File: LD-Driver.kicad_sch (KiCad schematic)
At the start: 2 parts, among them J1 BASYS3, U1 MCP4728

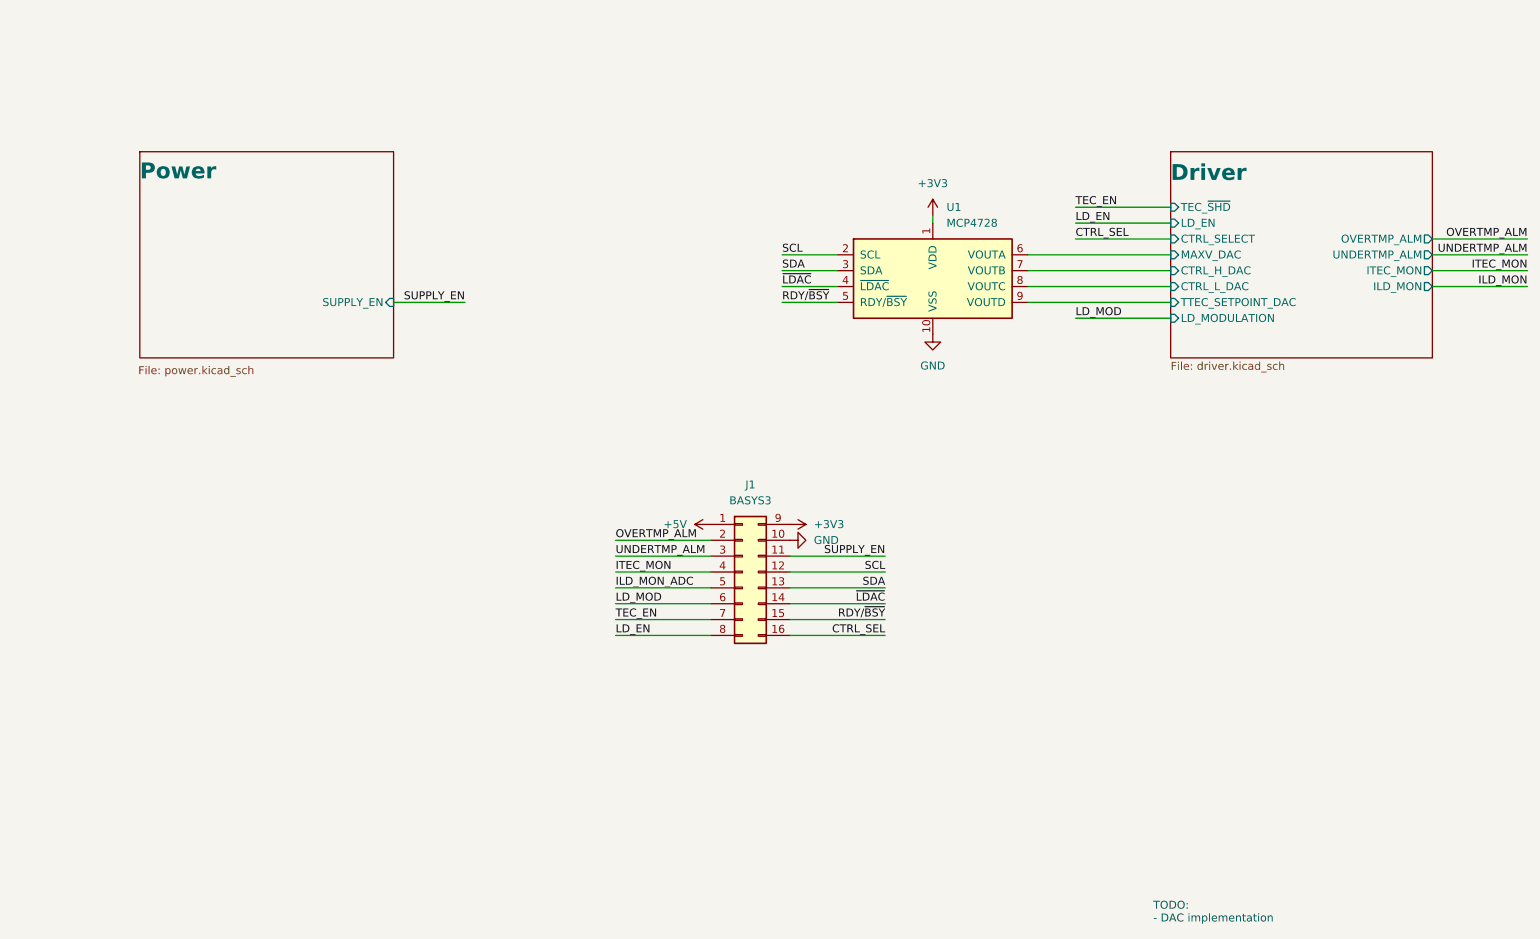
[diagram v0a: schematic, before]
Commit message: update PCB: fixed buck layout, concept layout for LD driver with LT3743
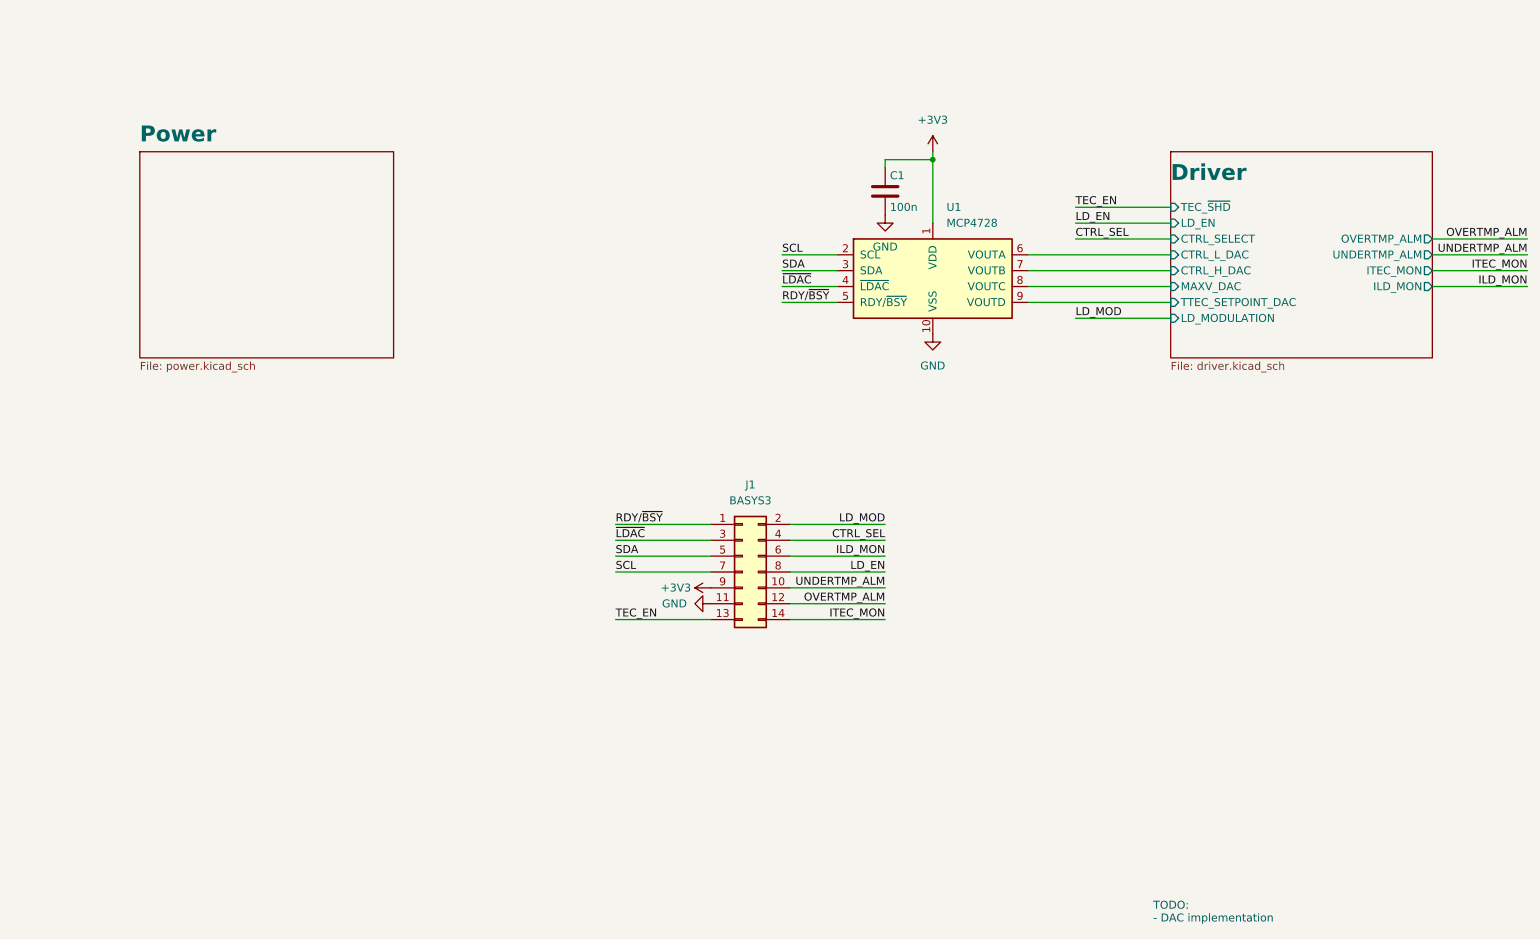
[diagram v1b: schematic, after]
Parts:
- added C1: 100n, Capacitor_SMD:C_0805_2012Metric, symbol Device:C
- J1: footprint Connector_PinHeader_2.54mm:PinHeader_2x08_P2.54mm_Horizontal -> Connector_PinHeader_2.54mm:PinHeader_2x07_P2.54mm_Horizontal; symbol Connector_Generic:Conn_02x08_Top_Bottom -> Connector_Generic:Conn_02x07_Odd_Even
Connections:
- net +5V is gone; now on net RDY/~{BSY}: J1.1 (Pin_1)
- net ILD_MON_ADC is gone; now on net SDA: J1.5 (Pin_5)
- net SUPPLY_EN is gone; now on net GND: J1.11 (Pin_11)
- net +3V3: now also C1.1
- net CTRL_SEL: now also J1.4 (Pin_4); no longer J1.16 (Pin_16)
- net Driver/CTRL_L_DAC: now also U1.6 (VOUTA); no longer U1.8 (VOUTC)
- net Driver/MAXV_DAC: now also U1.8 (VOUTC); no longer U1.6 (VOUTA)
- net GND: now also C1.2; no longer J1.10 (Pin_10)
- net ILD_MON: now also J1.6 (Pin_6)
- net ITEC_MON: now also J1.14 (Pin_14); no longer J1.4 (Pin_4)
- net LD_MOD: now also J1.2 (Pin_2); no longer J1.6 (Pin_6)
- net OVERTMP_ALM: now also J1.12 (Pin_12); no longer J1.2 (Pin_2)
- net RDY/~{BSY}: no longer J1.15 (Pin_15)
- net SCL: now also J1.7 (Pin_7); no longer J1.12 (Pin_12)
- net SDA: no longer J1.13 (Pin_13)
- net TEC_EN: now also J1.13 (Pin_13); no longer J1.7 (Pin_7)
- net UNDERTMP_ALM: now also J1.10 (Pin_10); no longer J1.3 (Pin_3)
- net ~{LDAC}: now also J1.3 (Pin_3); no longer J1.14 (Pin_14)
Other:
- sheet Power ports: added none; removed SUPPLY_EN

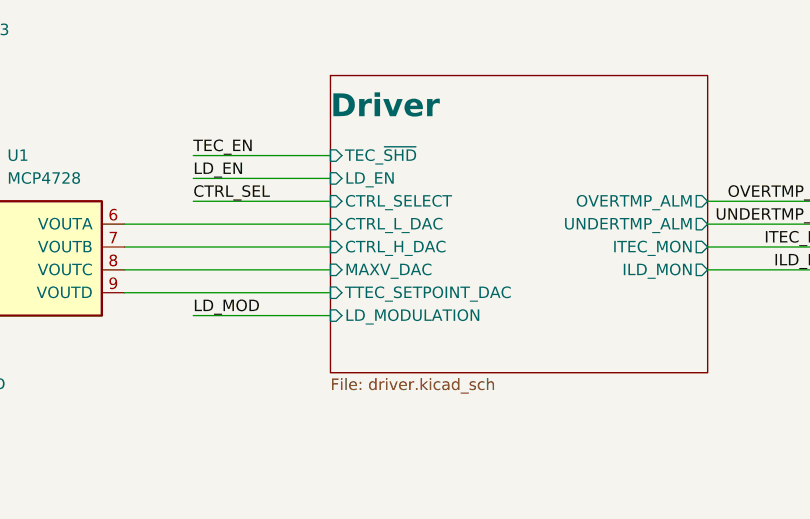
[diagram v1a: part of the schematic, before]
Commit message: PCB routing completed, started uniforming components for smaller BOM
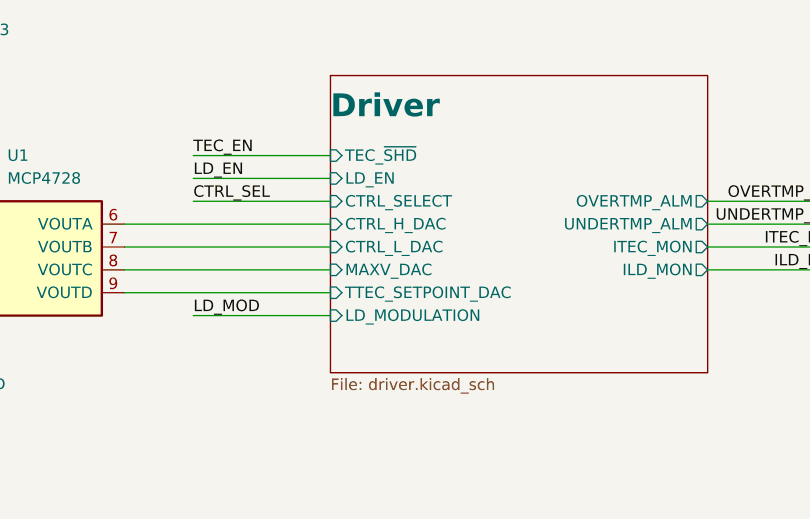
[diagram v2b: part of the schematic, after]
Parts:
- C1: footprint Capacitor_SMD:C_0805_2012Metric -> Capacitor_SMD:C_0603_1608Metric; Voltage Rating 25V -> 6V3
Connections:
- net Driver/CTRL_H_DAC: now also U1.6 (VOUTA); no longer U1.7 (VOUTB)
- net Driver/CTRL_L_DAC: now also U1.7 (VOUTB); no longer U1.6 (VOUTA)
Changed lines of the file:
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@@
+			)
+		)
+		(property "Sim.Device" ""
+			(at 171.45 67.31 0)
+			(effects
+				(font
+					(size 1.27 1.27)
+				)
+				(hide yes)
+			)
+		)
+		(property "Sim.Pins" ""
+			(at 171.45 67.31 0)
+			(effects
+				(font
+					(size 1.27 1.27)
+				)
+				(hide yes)
+			)
+		)
+		(property "Sim.Type" ""
+			(at 171.45 67.31 0)
+			(effects
+				(font
+					(size 1.27 1.27)
+				)
+				(hide yes)
 			)
 		)
@@
 			)
 		)
-		(property "Footprint" "Capacitor_SMD:C_0805_2012Metric"
+		(property "Footprint" "Capacitor_SMD:C_0603_1608Metric"
 			(at 164.7952 58.42 0)
 			(effects
@@
 			)
 		)
-		(property "Voltage Rating" "25V"
+		(property "Voltage Rating" "6V3"
+			(at 163.83 54.61 0)
+			(effects
+				(font
+					(size 1.27 1.27)
+				)
+				(hide yes)
+			)
+		)
+		(property "Sim.Device" ""
+			(at 163.83 54.61 0)
+			(effects
+				(font
+					(size 1.27 1.27)
+				)
+				(hide yes)
+			)
+		)
+		(property "Sim.Pins" ""
+			(at 163.83 54.61 0)
+			(effects
+				(font
+					(size 1.27 1.27)
+				)
+				(hide yes)
+			)
+		)
+		(property "Sim.Type" ""
 			(at 163.83 54.61 0)
 			(effects
@@
 			)
 		)
+		(property "Sim.Device" ""
+			(at 140.97 115.57 0)
+			(effects
+				(font
+					(size 1.27 1.27)
+				)
+				(hide yes)
+			)
+		)
+		(property "Sim.Pins" ""
+			(at 140.97 115.57 0)
+			(effects
+				(font
+					(size 1.27 1.27)
+				)
+				(hide yes)
+			)
+		)
+		(property "Sim.Type" ""
+			(at 140.97 115.57 0)
+			(effects
+				(font
+					(size 1.27 1.27)
+				)
+				(hide yes)
+			)
+		)
 		(pin "9"
 		)
@@
 		)
 		(pin "CTRL_H_DAC" input
+			(at 209.55 64.77 180)
+			(effects
+				(font
+					(size 1.27 1.27)
+				)
+				(justify left)
+			)
+		)
+		(pin "CTRL_L_DAC" input
 			(at 209.55 67.31 180)
 			(effects
 				(font
-					(size 1.27 1.27)
-				)
-				(justify left)
-			)
-		)
-		(pin "CTRL_L_DAC" input
-			(at 209.55 64.77 180)
-			(effects
-				(font

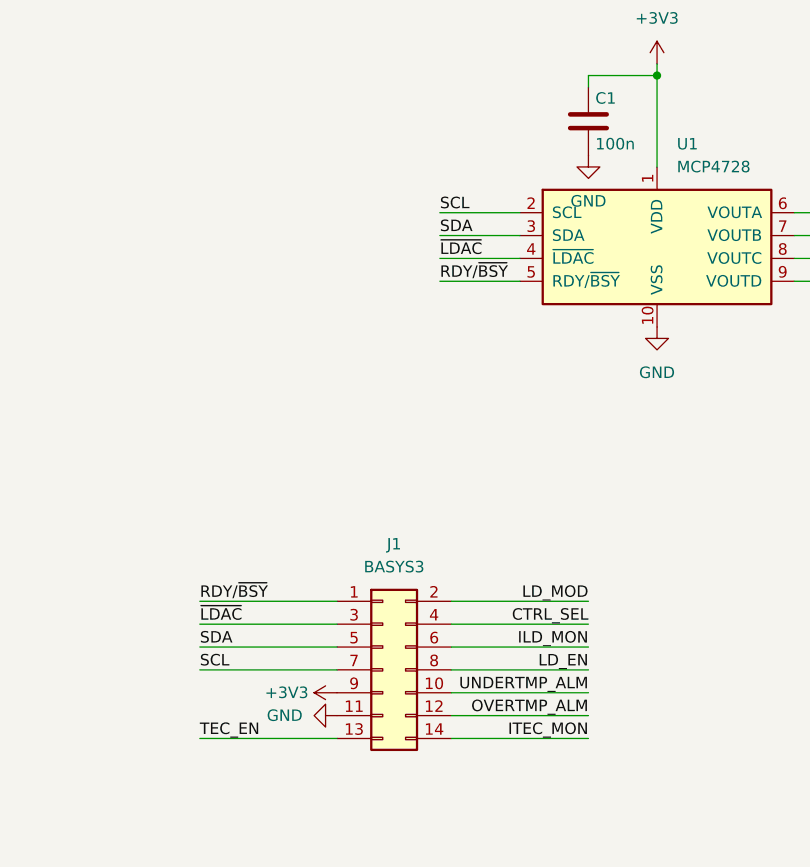
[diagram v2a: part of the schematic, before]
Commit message: feat: made possible to swap butterfly pins for compatibility
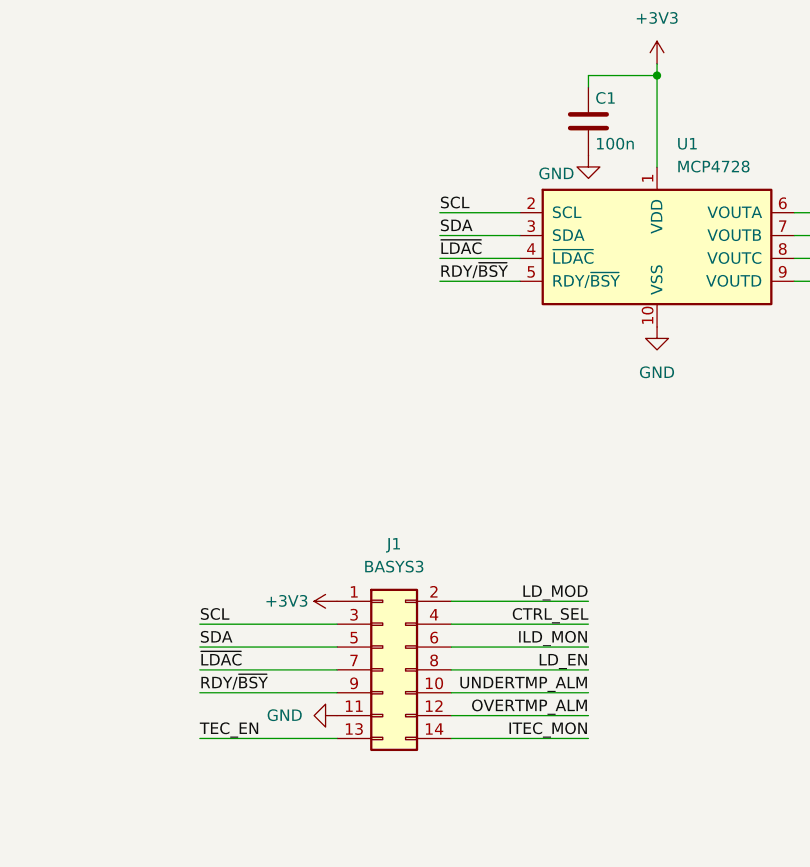
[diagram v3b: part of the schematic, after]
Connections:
- net +3V3: now also J1.1 (Pin_1); no longer J1.9 (Pin_9)
- net RDY/~{BSY}: now also J1.9 (Pin_9); no longer J1.1 (Pin_1)
- net SCL: now also J1.3 (Pin_3); no longer J1.7 (Pin_7)
- net ~{LDAC}: now also J1.7 (Pin_7); no longer J1.3 (Pin_3)

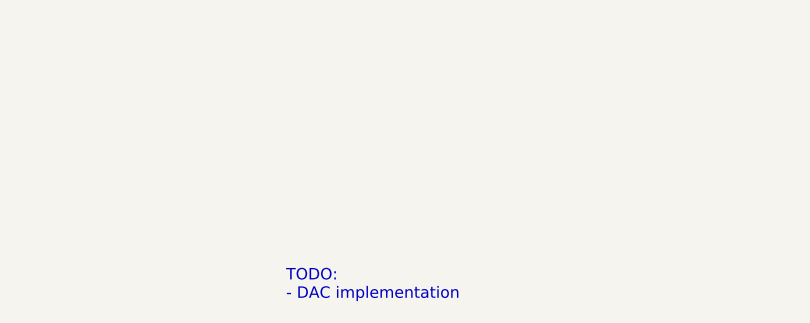
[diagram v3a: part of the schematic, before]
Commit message: fix: small corrections to the pcb, added PNs and store link to mouser for each component
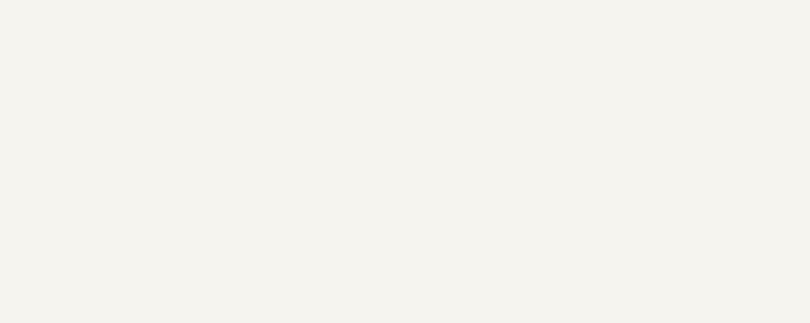
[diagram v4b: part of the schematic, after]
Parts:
- C1: PN (none) -> CL10B104KB8NNND; Store Link (none) -> https://www.mouser.it/ProductDetail/Samsung-Electro-Mechani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
- J1: now left out of the parts list
- U1: PN (none) -> MCP4728-E/UN; Store Link (none) -> https://www.mouser.it/ProductDetail/Microchip-Technology/MC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
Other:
- note removed: "TODO: - DAC implementation"
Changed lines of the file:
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@@
-		)
-	)
-	(text "TODO:\n- DAC implementation"
-		(exclude_from_sim no)
-		(at 206.756 170.18 0)
-		(effects
-			(font
-				(size 1.27 1.27)
-			)
-			(justify left)
 		)
 	)
@@
 			)
 		)
+		(property "PN" " MCP4728-E/UN "
+			(at 171.45 67.31 0)
+			(effects
+				(font
+					(size 1.27 1.27)
+				)
+				(hide yes)
+			)
+		)
+		(property "Store Link" "https://www.mouser.it/ProductDetail/Microchip-Technology/MCP4728-E-UN?qs=E6wAi2XWqcP2zTenScklGA%3D%3D"
+			(at 171.45 67.31 0)
+			(effects
+				(font
+					(size 1.27 1.27)
+				)
+				(hide yes)
+			)
+		)
 		(pin "8"
 		)
@@
 			)
 		)
+		(property "PN" " CL10B104KB8NNND "
+			(at 163.83 54.61 0)
+			(effects
+				(font
+					(size 1.27 1.27)
+				)
+				(hide yes)
+			)
+		)
+		(property "Store Link" "https://www.mouser.it/ProductDetail/Samsung-Electro-Mechanics/CL10B104KB8NNND?qs=349EhDEZ59pgcFJT%2FYAROA%3D%3D"
+			(at 163.83 54.61 0)
+			(effects
+				(font
+					(size 1.27 1.27)
+				)
+				(hide yes)
+			)
+		)
 		(pin "1"
 		)
@@
 		(unit 1)
 		(exclude_from_sim no)
-		(in_bom yes)
+		(in_bom no)
 		(on_board yes)
 		(dnp no)
